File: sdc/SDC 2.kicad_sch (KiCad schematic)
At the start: 101 parts, among them J1 BSPD_LED, J10 BMS_LED, J11 BSPD_Fault, J12 IMD_Fault, J13 BMS_Fault, J14 12V PWR, J15 SDC_IN, J16 SDC_OUT, J2 IMD_LED, J3 BMS_LED, J4 SW_Fault, J5 BSPD_BTN, J6 IMD_BTN, J7 BMS_BTN, J8 BSPD_LED, J9 IMD_LED, K1 G2RL-2A, K2 G2RL-2A, K3 G2RL-2A, K4 G2RL-2A, Q1 2N7002, Q2 2N7002, Q3 2N7002, Q4 2N7002, Q5 2N7002, Q6 2N7002, U1 VOM618AT, U10 AP2204K-ADJ, U2 VOM618AT, U3 TLV2371DBV, U4 TLV2371DBV, U6 VOM618AT, U7 VOM618AT, U8 TLV2371DBV, U9 AP2204K-ADJ

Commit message: SDC add pinheader
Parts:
- added J17, J18: Conn_01x15_Pin, symbol Connector:Conn_01x15_Pin
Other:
- note removed: "BJT->MOS 電源電阻換10k LDO"
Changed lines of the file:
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@@
     (stroke (width 0) (type default))
   )
-  (text "BJT->MOS\n電源電阻換10k\nLDO" (at 232.41 176.53 0)
-    (effects (font (size 1.27 1.27)) (justify left bottom))
-  )
   (global_label "BMS_LED" (shape input) (at 224.79 78.105 180) (fields_autoplaced)
     (effects (font (size 1.27 1.27)) (justify right))
@@
     )
   )
+  (symbol (lib_id "Connector:Conn_01x15_Pin") (at 223.52 36.83 0) (unit 1)
+    (in_bom yes) (on_board yes) (dnp no) (fields_autoplaced)
+    (property "Reference" "J18" (at 224.155 13.97 0)
+      (effects (font (size 1.27 1.27)))
+    )
+    (property "Value" "Conn_01x15_Pin" (at 224.155 16.51 0)
+      (effects (font (size 1.27 1.27)))
+    )
+    (property "Footprint" "" (at 223.52 36.83 0)
+      (effects (font (size 1.27 1.27)) hide)
+    )
+    (property "Datasheet" "~" (at 223.52 36.83 0)
+      (effects (font (size 1.27 1.27)) hide)
+    )
+    (pin "10")
+    (pin "14")
+    (pin "1")
+    (pin "11")
+    (pin "8")
+    (pin "5")
+    (pin "7")
+    (pin "3")
+    (pin "6")
+    (pin "4")
+    (pin "15")
+    (pin "2")
+    (pin "13")
+    (pin "9")
+    (pin "12")
+    (instances
+      (project "SDC 2"
+        (path "/5dfd26ec-2ec4-449e-a223-7366b4f866d8"
+          (reference "J18") (unit 1)
+        )
+      )
+    )
+  )
   (symbol (lib_id "power:GND") (at 144.78 190.5 0) (unit 1)
     (in_bom yes) (on_board yes) (dnp no) (fields_autoplaced)
@@
         )
       )
+    )
+  )
+  (symbol (lib_id "Connector:Conn_01x15_Pin") (at 204.47 36.83 0) (unit 1)
+    (in_bom yes) (on_board yes) (dnp no) (fields_autoplaced)
+    (property "Reference" "J17" (at 205.105 13.97 0)
+      (effects (font (size 1.27 1.27)))
+    )
+    (property "Value" "Conn_01x15_Pin" (at 205.105 16.51 0)
+      (effects (font (size 1.27 1.27)))
+    )
+    (property "Footprint" "" (at 204.47 36.83 0)
+      (effects (font (size 1.27 1.27)) hide)
+    )
+    (property "Datasheet" "~" (at 204.47 36.83 0)
+      (effects (font (size 1.27 1.27)) hide)
+    )
+    (pin "10")
+    (pin "14")
+    (pin "1")
+    (pin "11")
+    (pin "8")
+    (pin "5")
+    (pin "7")
+    (pin "3")
+    (pin "6")
+    (pin "4")
+    (pin "15")
+    (pin "2")
+    (pin "13")
+    (pin "9")
+    (pin "12")
+    (instances
+      (project "SDC 2"
+        (path "/5dfd26ec-2ec4-449e-a223-7366b4f866d8"
+          (reference "J17") (unit 1)
+        )
+      )

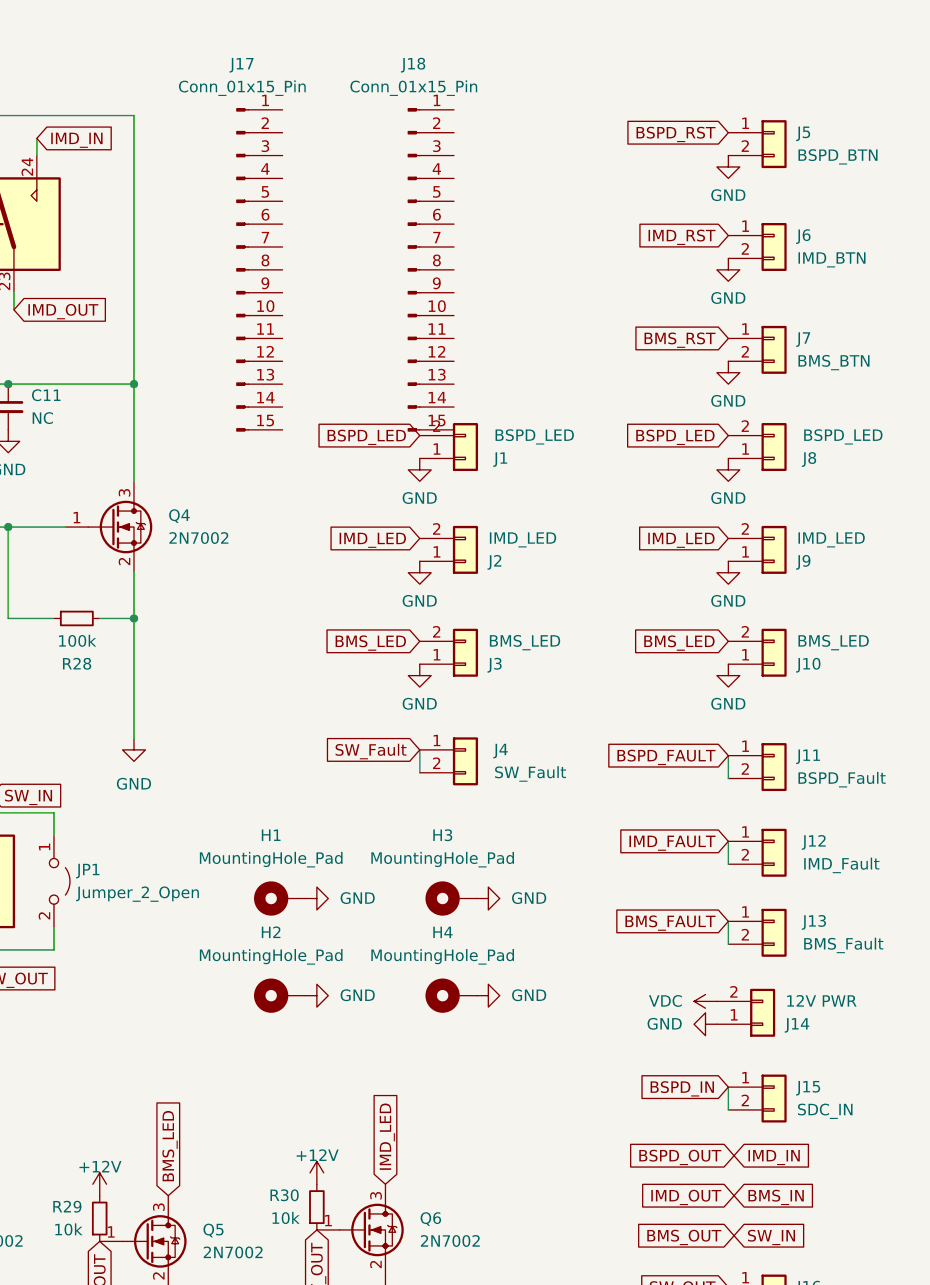
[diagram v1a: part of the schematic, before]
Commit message: Change JST to pin header
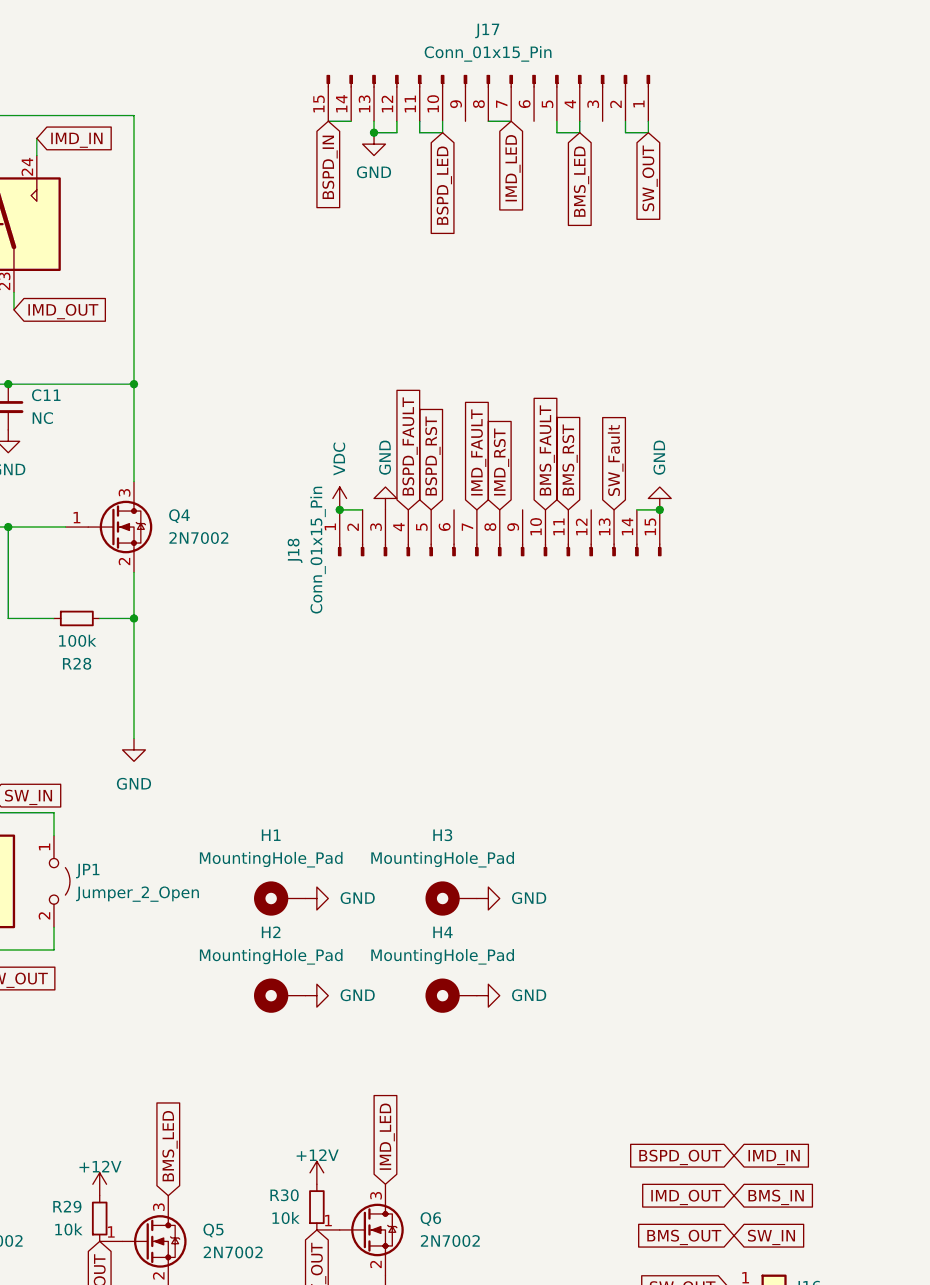
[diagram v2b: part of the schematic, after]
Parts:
- removed J1, J8: BSPD_LED, Connector_JST:JST_XH_B2B-XH-A_1x02_P2.50mm_Vertical, symbol Connector_Generic:Conn_01x02
- removed J10, J3: BMS_LED, Connector_JST:JST_XH_B2B-XH-A_1x02_P2.50mm_Vertical, symbol Connector_Generic:Conn_01x02
- removed J11: BSPD_Fault, Connector_JST:JST_XH_B2B-XH-A_1x02_P2.50mm_Vertical, symbol Connector_Generic:Conn_01x02
- removed J12: IMD_Fault, Connector_JST:JST_XH_B2B-XH-A_1x02_P2.50mm_Vertical, symbol Connector_Generic:Conn_01x02
- removed J13: BMS_Fault, Connector_JST:JST_XH_B2B-XH-A_1x02_P2.50mm_Vertical, symbol Connector_Generic:Conn_01x02
- removed J14: 12V PWR, Connector_JST:JST_XH_B2B-XH-A_1x02_P2.50mm_Vertical, symbol Connector_Generic:Conn_01x02
- removed J15: SDC_IN, Connector_JST:JST_XH_B2B-XH-A_1x02_P2.50mm_Vertical, symbol Connector_Generic:Conn_01x02
- removed J2, J9: IMD_LED, Connector_JST:JST_XH_B2B-XH-A_1x02_P2.50mm_Vertical, symbol Connector_Generic:Conn_01x02
- removed J4: SW_Fault, Connector_JST:JST_XH_B2B-XH-A_1x02_P2.50mm_Vertical, symbol Connector_Generic:Conn_01x02
- removed J5: BSPD_BTN, Connector_JST:JST_XH_B2B-XH-A_1x02_P2.50mm_Vertical, symbol Connector_Generic:Conn_01x02
- removed J6: IMD_BTN, Connector_JST:JST_XH_B2B-XH-A_1x02_P2.50mm_Vertical, symbol Connector_Generic:Conn_01x02
- removed J7: BMS_BTN, Connector_JST:JST_XH_B2B-XH-A_1x02_P2.50mm_Vertical, symbol Connector_Generic:Conn_01x02
- J17, J18: footprint (none) -> Connector_PinHeader_2.54mm:PinHeader_1x15_P2.54mm_Vertical
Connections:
- net BMS_FAULT: now also J18.10 (Pin_10)
- net BMS_LED: now also J17.4 (Pin_4), J17.5 (Pin_5)
- net BMS_RST: now also J18.11 (Pin_11)
- net BSPD_FAULT: now also J18.4 (Pin_4)
- net BSPD_IN: now also J17.14 (Pin_14), J17.15 (Pin_15)
- net BSPD_LED: now also J17.10 (Pin_10), J17.11 (Pin_11)
- net BSPD_RST: now also J18.5 (Pin_5)
- net GND: now also J17.12 (Pin_12), J17.13 (Pin_13), J18.14 (Pin_14), J18.15 (Pin_15), J18.3 (Pin_3)
- net IMD_FAULT: now also J18.7 (Pin_7)
- net IMD_LED: now also J17.7 (Pin_7), J17.8 (Pin_8)
- net IMD_RST: now also J18.8 (Pin_8)
- net SW_Fault: now also J18.13 (Pin_13)
- net SW_OUT: now also J17.1 (Pin_1), J17.2 (Pin_2)
- net VDC: now also J18.1 (Pin_1), J18.2 (Pin_2)
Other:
- moved on the sheet: J17, J18

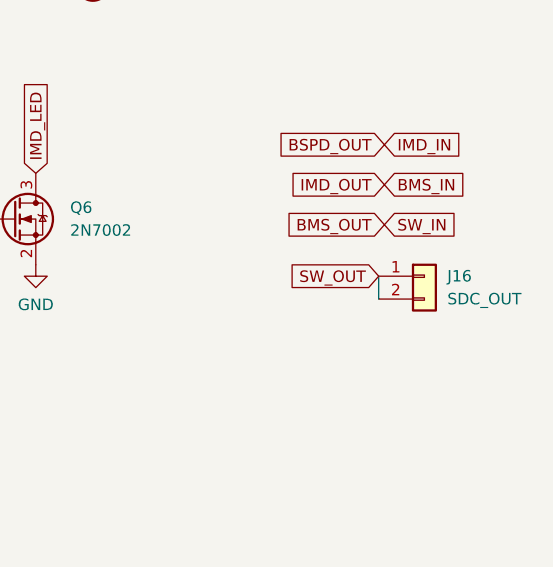
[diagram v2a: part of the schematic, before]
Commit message: Change JST to pinheader
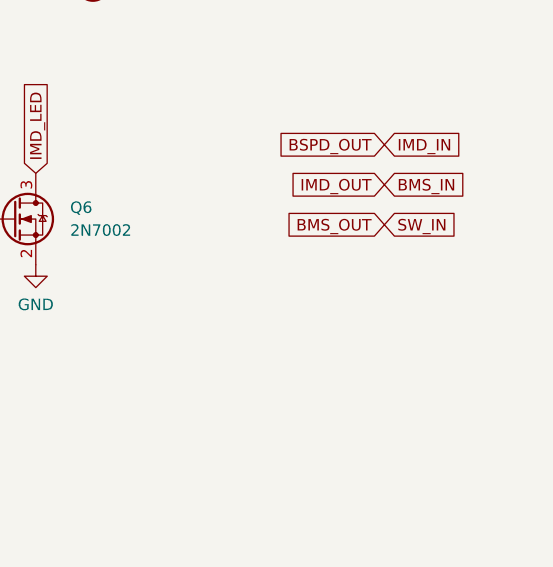
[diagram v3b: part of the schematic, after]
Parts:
- removed J16: SDC_OUT, Connector_JST:JST_XH_B2B-XH-A_1x02_P2.50mm_Vertical, symbol Connector_Generic:Conn_01x02
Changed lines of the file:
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@@
-    (stroke (width 0) (type default))
-  )
-  (wire (pts (xy 259.08 149.86) (xy 259.08 152.4))
     (stroke (width 0) (type default))
   )
@@
     (property "Intersheetrefs" "${INTERSHEET_REFS}" (at 231.14 50.7176 90)
       (effects (font (size 1.27 1.27)) (justify left) hide)
-    )
-  )
-  (global_label "SW_OUT" (shape input) (at 259.08 149.86 180) (fields_autoplaced)
-    (effects (font (size 1.27 1.27)) (justify right))
-    (property "Intersheetrefs" "${INTERSHEET_REFS}" (at 248.8377 149.86 0)
-      (effects (font (size 1.27 1.27)) (justify right) hide)
     )
   )
@@
         )
       )
-    )
-  )
-  (symbol (lib_id "Connector_Generic:Conn_01x02") (at 264.16 149.86 0) (unit 1)
-    (in_bom yes) (on_board yes) (dnp no) (fields_autoplaced)
-    (property "Reference" "J16" (at 266.7 149.86 0)
-      (effects (font (size 1.27 1.27)) (justify left))
-    )
-    (property "Value" "SDC_OUT" (at 266.7 152.4 0)
-      (effects (font (size 1.27 1.27)) (justify left))
-    )
-    (property "Footprint" "Connector_JST:JST_XH_B2B-XH-A_1x02_P2.50mm_Vertical" (at 264.16 149.86 0)
-      (effects (font (size 1.27 1.27)) hide)
-    )
-    (property "Datasheet" "~" (at 264.16 149.86 0)
-      (effects (font (size 1.27 1.27)) hide)
-    )
-    (property "Sim.Enable" "0" (at 264.16 149.86 0)
-      (effects (font (size 1.27 1.27)) hide)
-    )
-    (pin "1")
-    (pin "2")
-    (instances
-      (project "SDC 2"
-        (path "/5dfd26ec-2ec4-449e-a223-7366b4f866d8"
-          (reference "J16") (unit 1)
-        )
-      )

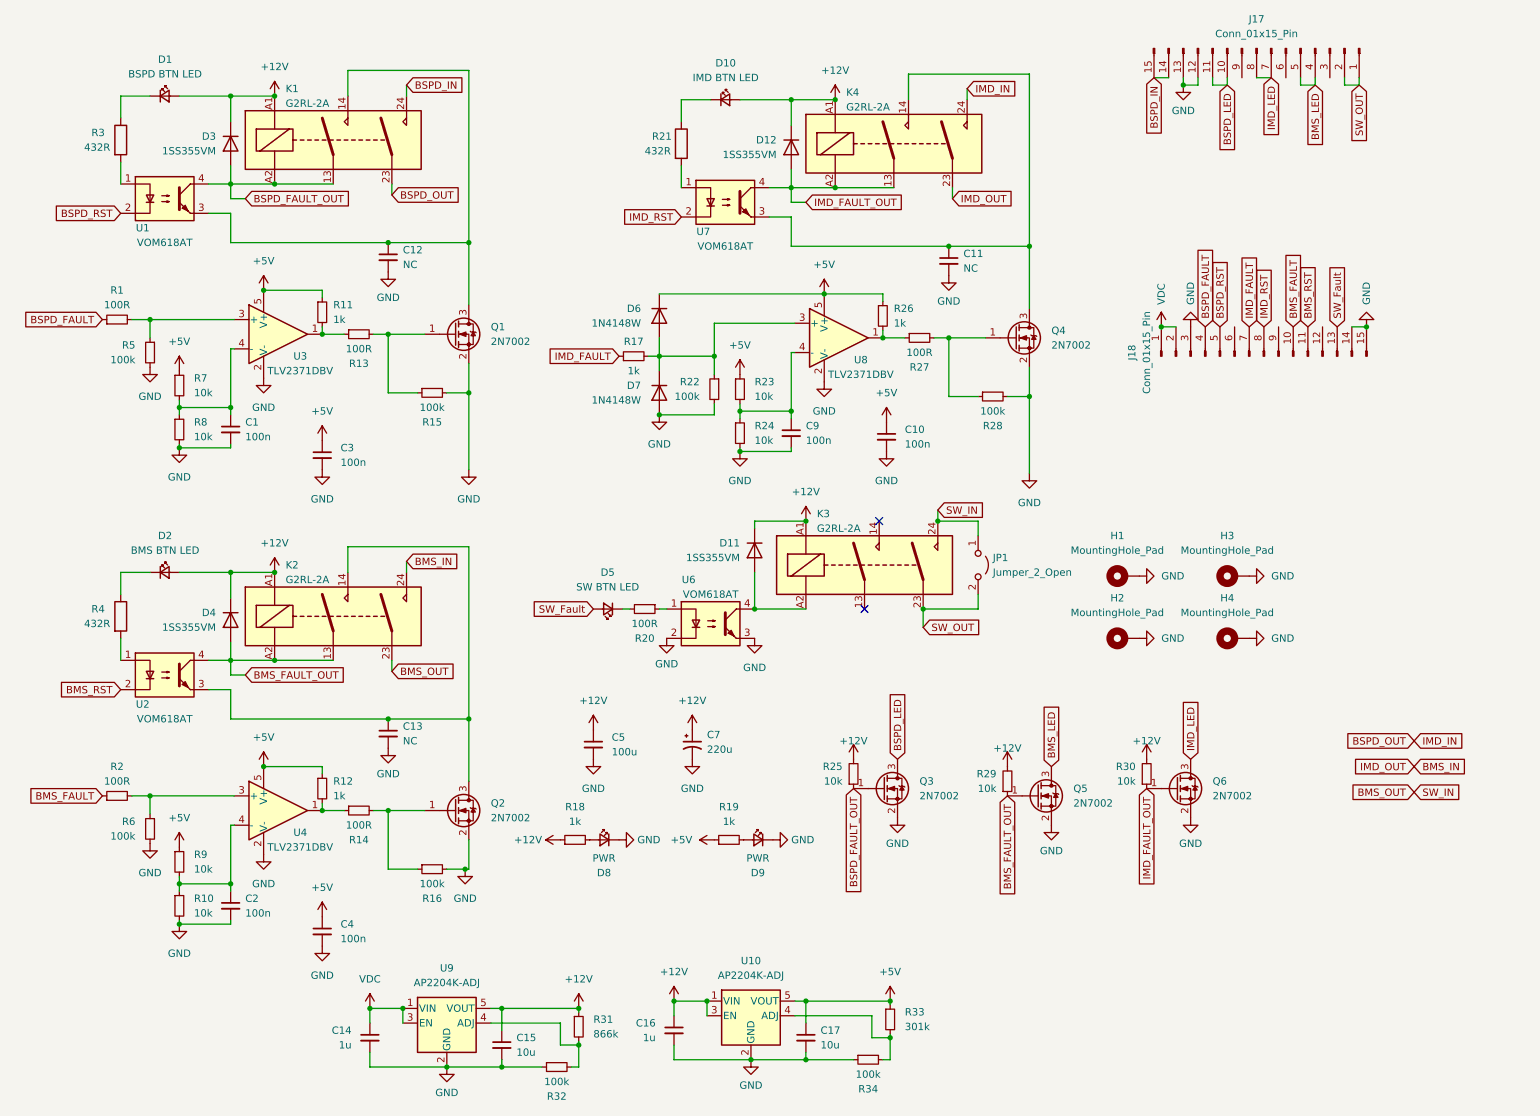
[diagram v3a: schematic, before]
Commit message: feat: use 2x10 pin
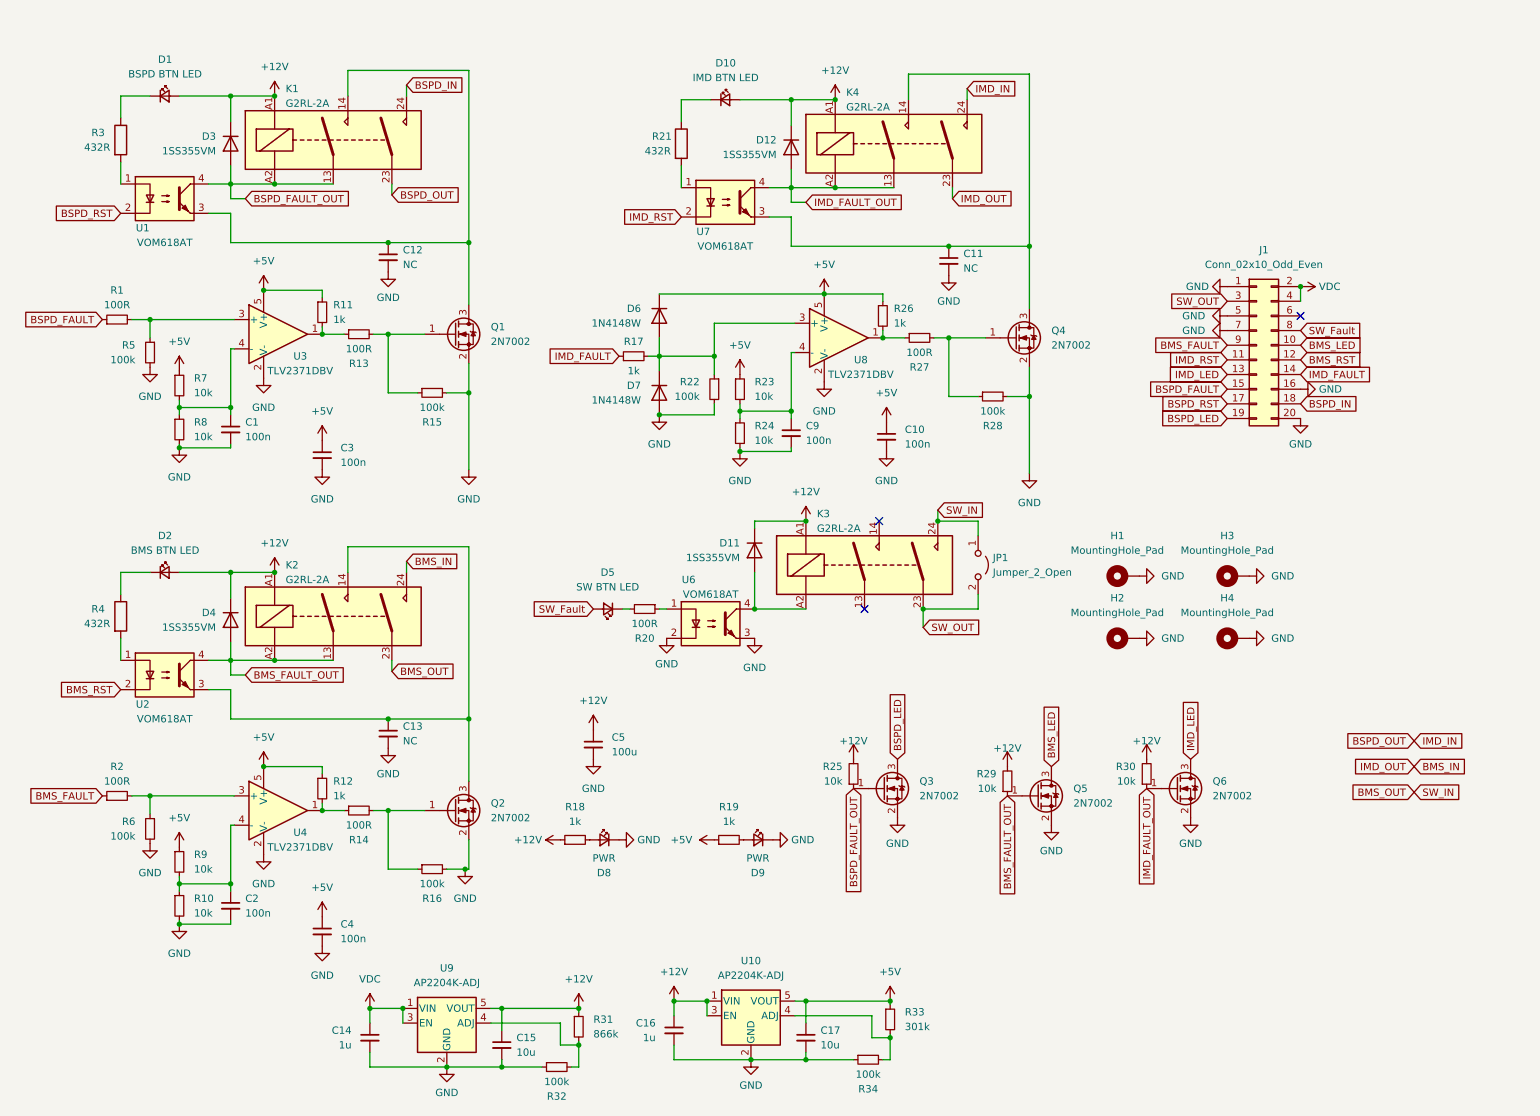
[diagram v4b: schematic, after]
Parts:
- removed C7: 220u, Capacitor_THT:C_Radial_D12.5mm_H25.0mm_P5.00mm, symbol Device:C_Polarized_Small_US
- removed J17, J18: Conn_01x15_Pin, Connector_PinHeader_2.54mm:PinHeader_1x15_P2.54mm_Vertical, symbol Connector:Conn_01x15_Pin
- added J1: Conn_02x10_Odd_Even, Connector_PinHeader_2.54mm:PinHeader_2x10_P2.54mm_Vertical, symbol Connector_Generic:Conn_02x10_Odd_Even
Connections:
- net BMS_FAULT: now also J1.9 (Pin_9)
- net BMS_LED: now also J1.10 (Pin_10)
- net BMS_RST: now also J1.12 (Pin_12)
- net BSPD_FAULT: now also J1.15 (Pin_15)
- net BSPD_IN: now also J1.18 (Pin_18)
- net BSPD_LED: now also J1.19 (Pin_19)
- net BSPD_RST: now also J1.17 (Pin_17)
- net GND: now also J1.1 (Pin_1), J1.16 (Pin_16), J1.20 (Pin_20), J1.5 (Pin_5), J1.7 (Pin_7)
- net IMD_FAULT: now also J1.14 (Pin_14)
- net IMD_LED: now also J1.13 (Pin_13)
- net IMD_RST: now also J1.11 (Pin_11)
- net SW_Fault: now also J1.8 (Pin_8)
- net SW_OUT: now also J1.3 (Pin_3)
- net VDC: now also J1.2 (Pin_2), J1.4 (Pin_4)
- no-connect marks 2 -> 3
